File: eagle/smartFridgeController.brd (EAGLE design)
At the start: 35.9 x 45.7 mm, 12 parts

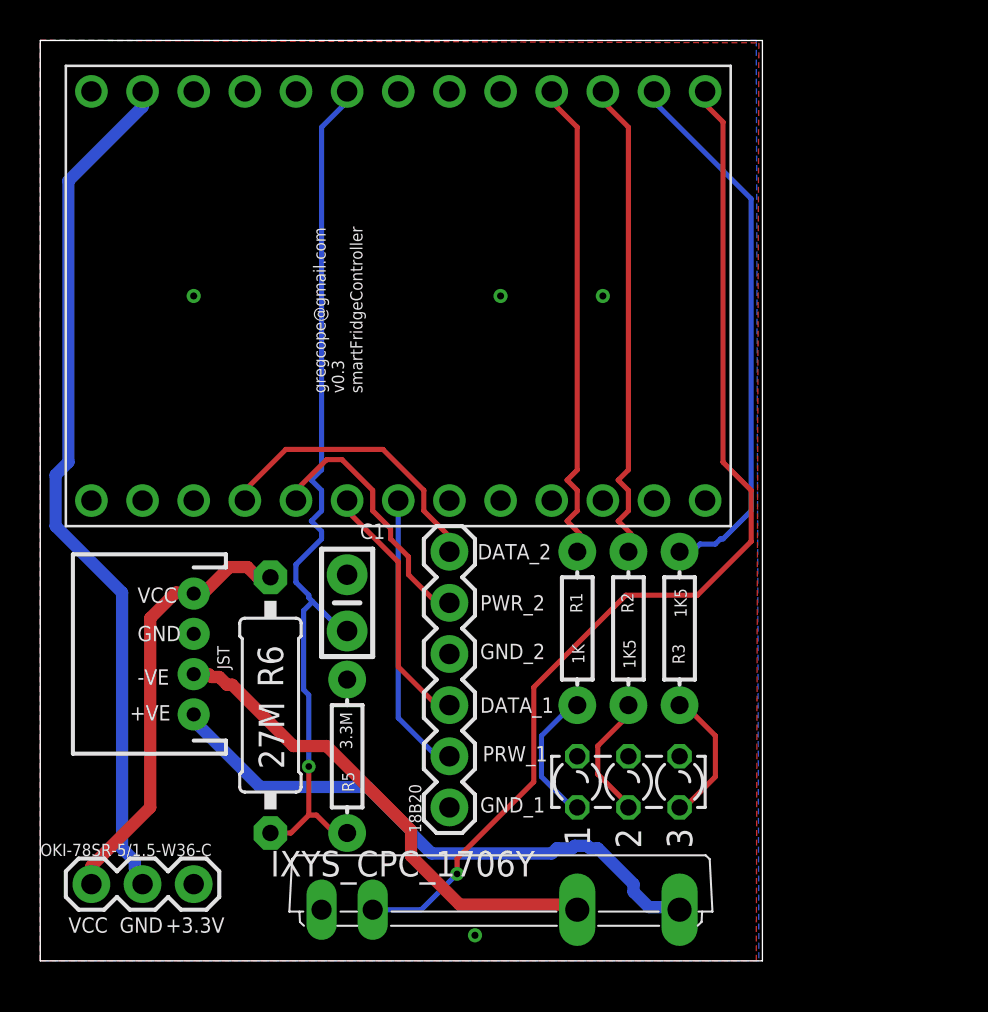
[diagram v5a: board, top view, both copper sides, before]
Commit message: added RGB LED
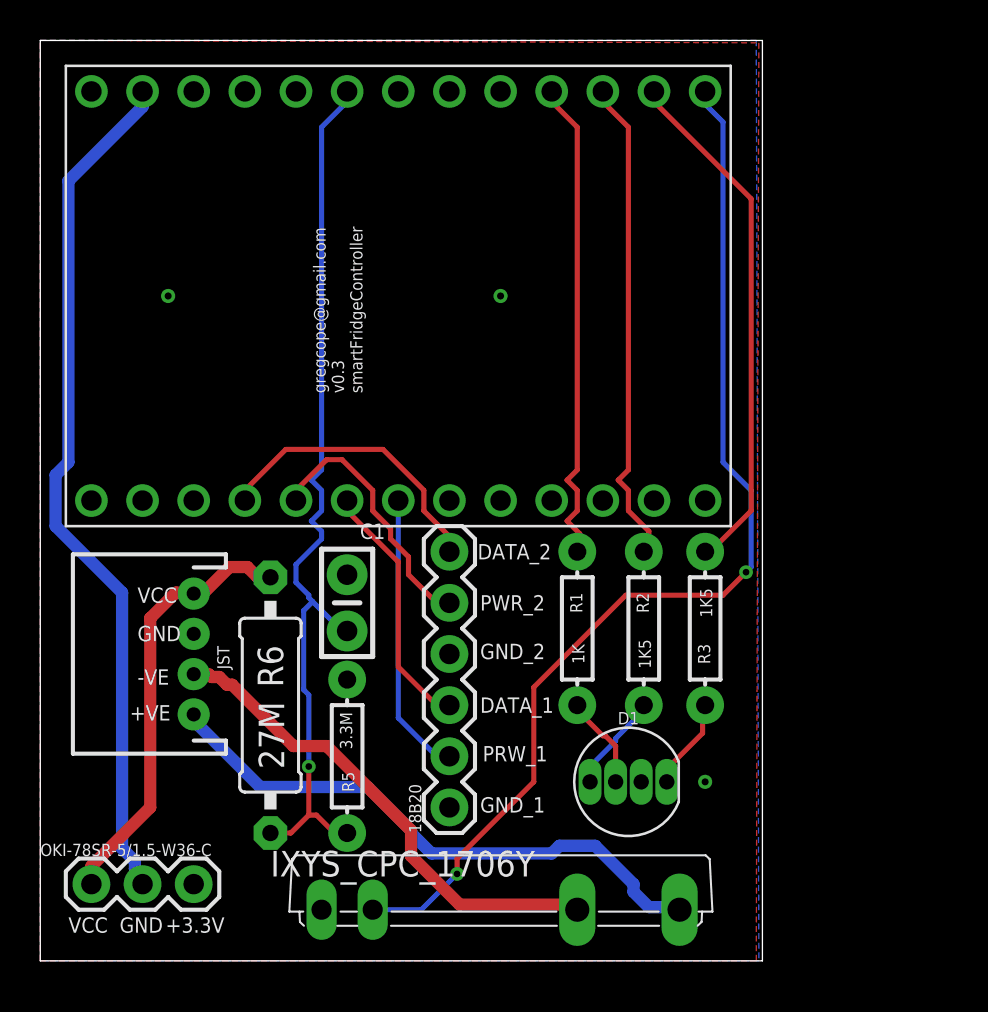
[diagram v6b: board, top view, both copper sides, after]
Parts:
- removed DZ1: LZR183, led:LZR183
- added D1: CLEAR, SparkFun-LED:LED-RGB-THRU
- moved R3 1.27 mm to (31.8, 16.5)
- moved R2 0.76 mm to (28.7, 16.5)
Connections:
- net D16_LED_YELLOW_PIN renamed D16_LED_BLUE_PIN
- net GND: no longer DZ1.K1, DZ1.K2, DZ1.K3
- net N$1: now also D1.1, R3.P$1; no longer DZ1.A1, R1.P$1
- net N$2: now also D1.4; no longer DZ1.A2
- net N$3: now also D1.3, R1.P$1; no longer DZ1.A3, R3.P$1
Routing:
- net N$1: track 6.85 -> 4.60 mm
- net N$3: track 6.85 -> 4.67 mm
- net N$2: track 6.34 -> 4.91 mm
- net D15_LED_RED_PIN: track 27.2 -> 26.0 mm
- net D14_RELAY_PIN: track 52.9 -> 53.6 mm, vias 1 -> 2

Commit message: simpler route, gnd pour
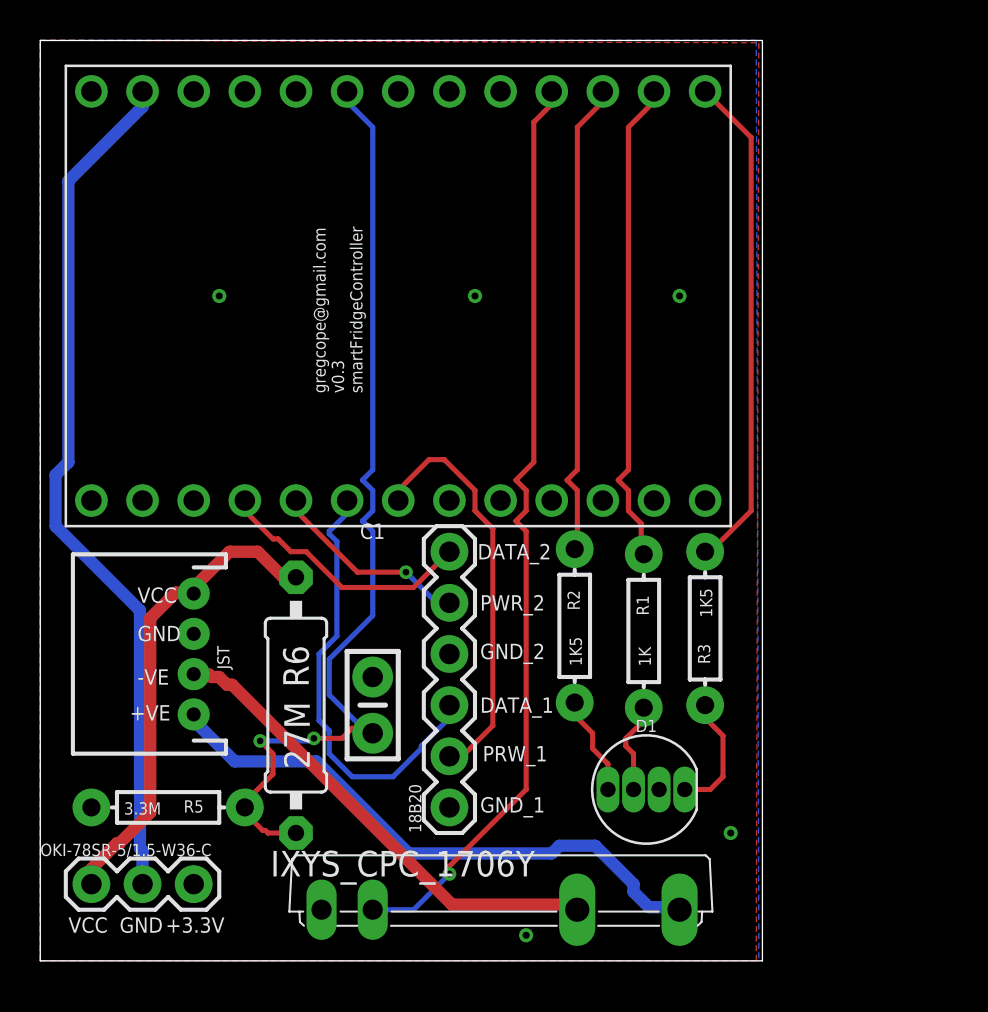
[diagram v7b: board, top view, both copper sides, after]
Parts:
- moved R5 9.25 mm to (5.08, 7.62), turned to 0 degrees
- moved C1 5.24 mm to (15.2, 12.7)
- moved R2 3.43 mm to (25.3, 16.6)
- moved R1 3.30 mm to (28.7, 16.4)
- moved R6 1.27 mm to (11.4, 12.7)
- moved D1 0.97 mm to (28.8, 8.51)
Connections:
- removed net D14_RELAY_PIN: IXYS_CPC_1706Y.2, U$2.A0
- removed net D15_LED_RED_PIN: R3.P$2, U$2.A1
- removed net D17_LED_GREEN_PIN: R1.P$2, U$2.A3
- new net D14_LED_RED_PIN: R3.P$2, U$2.A0
- new net D15_LED_GREEN_PIN: R1.P$2, U$2.A1
- new net D17_RELAY_PIN: IXYS_CPC_1706Y.2, U$2.A3
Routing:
- net D14_RELAY_PIN: track 53.6 -> 0.00 mm, vias 2 -> 0
- net D17_RELAY_PIN: track 0.00 -> 46.4 mm, vias 0 -> 1
- net D15_LED_RED_PIN: track 26.0 -> 0.00 mm
- net D14_LED_RED_PIN: track 0.00 -> 24.9 mm
- net D17_LED_GREEN_PIN: track 24.3 -> 0.00 mm
- net D15_LED_GREEN_PIN: track 0.00 -> 24.2 mm
- net D6_DS1_DATA: track 12.6 -> 22.0 mm
- net D7_DS1_PWR: track 14.1 -> 20.4 mm
- net A7_VCC_VD: track 45.3 -> 48.5 mm, vias 1 -> 2
- net D5_DS2_PWR: track 13.1 -> 10.0 mm, vias 0 -> 1
- net VCC: track 21.7 -> 23.8 mm
- net D4_DS2_DATA: track 14.7 -> 13.0 mm
- net N$1: track 4.60 -> 6.09 mm
- net -VE: track 24.6 -> 23.9 mm
- net D16_LED_BLUE_PIN: track 24.3 -> 23.7 mm

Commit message: New layout, 0.3
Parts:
- removed D1: CLEAR, SparkFun-LED:LED-RGB-THRU
- added STATUS_LED: CLEAR, SparkFun-LED:LED-RGB-THRU
- JST: value (none) -> 18B20
- moved R1 16.8 mm to (27.9, 33.1)
- moved R3 16.6 mm to (31.8, 33.1)
- moved R2 16.6 mm to (24.0, 33.1)
- moved 18B20 13.7 mm to (31.8, 12.7), turned to 180 degrees
- moved R5 13.6 mm to (15.4, 16.5), turned to 270 degrees
- moved C1 6.52 mm to (18.8, 18.2)
- moved IXYS_CPC_1706Y 4.58 mm to (24.1, 6.35)
- moved OKI-78SR-5/1.5-W36-C 3.76 mm to (2.03, 7.49)
- moved R6 1.27 mm to (11.4, 14.0)
- moved JST 1.27 mm to (5.08, 15.2)
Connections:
- net GND: now also STATUS_LED.2
- net N$1: now also STATUS_LED.1; no longer D1.1
- net N$2: now also STATUS_LED.4; no longer D1.4
- net N$3: now also STATUS_LED.3; no longer D1.3
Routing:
- net D17_RELAY_PIN: track 46.4 -> 73.2 mm, vias 1 -> 0
- net D14_LED_RED_PIN: track 24.9 -> 7.38 mm
- net D15_LED_GREEN_PIN: track 24.2 -> 6.75 mm
- net D16_LED_BLUE_PIN: track 23.7 -> 7.33 mm
- net N$3: track 4.59 -> 16.1 mm
- net N$2: track 5.00 -> 15.0 mm
- net D4_DS2_DATA: track 13.0 -> 20.1 mm
- net N$1: track 6.09 -> 12.7 mm
- net D5_DS2_PWR: track 10.0 -> 16.1 mm, vias 1 -> 0
- net VCC: track 23.8 -> 20.0 mm
- net VIN: track 42.9 -> 39.6 mm
- net D7_DS1_PWR: track 20.4 -> 17.3 mm
- net -VE: track 23.9 -> 26.1 mm
- net +VE: track 28.9 -> 30.8 mm
- net D6_DS1_DATA: track 22.0 -> 20.7 mm
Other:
- board size 35.9 x 45.7 mm -> 35.9 x 41.9 mm
